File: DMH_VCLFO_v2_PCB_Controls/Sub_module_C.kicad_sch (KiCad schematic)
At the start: 93 parts, among them J46 Conn_02x03_Odd_Even, J47 Conn_02x03_Odd_Even, J48 Conn_02x03_Odd_Even, J49 Conn_02x03_Odd_Even, J50 Conn_02x03_Odd_Even, J51 Conn_02x03_Odd_Even, Q29 BC548, Q30 BC548, Q31 MMBFJ113, Q32 MMBFJ113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

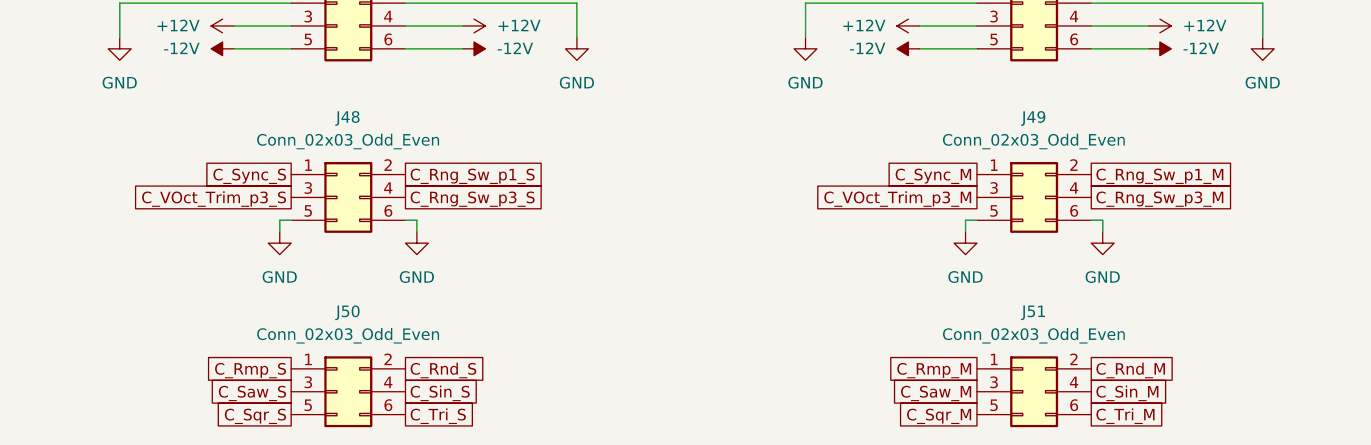
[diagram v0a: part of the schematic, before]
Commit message: Synced Controls PCB with Main
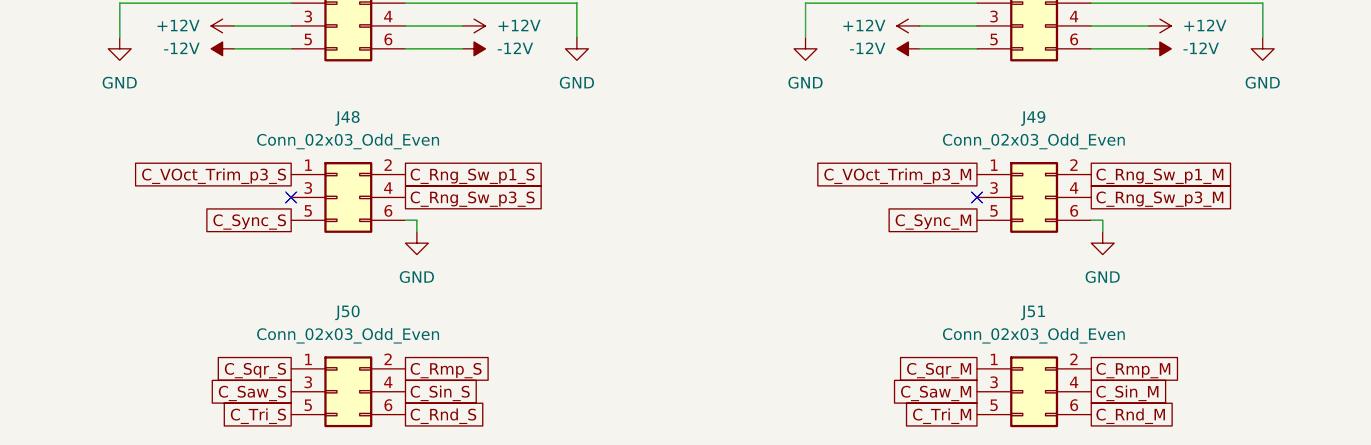
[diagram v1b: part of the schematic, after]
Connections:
- net C_Rmp_M: now also J51.2 (Pin_2); no longer J51.1 (Pin_1)
- net C_Rmp_S: now also J50.2 (Pin_2); no longer J50.1 (Pin_1)
- net C_Rnd_M: now also J51.6 (Pin_6); no longer J51.2 (Pin_2)
- net C_Rnd_S: now also J50.6 (Pin_6); no longer J50.2 (Pin_2)
- net C_Sqr_M: now also J51.1 (Pin_1); no longer J51.5 (Pin_5)
- net C_Sqr_S: now also J50.1 (Pin_1); no longer J50.5 (Pin_5)
- net C_Sync_M: now also J49.5 (Pin_5); no longer J49.1 (Pin_1)
- net C_Sync_S: now also J48.5 (Pin_5); no longer J48.1 (Pin_1)
- net C_Tri_M: now also J51.5 (Pin_5); no longer J51.6 (Pin_6)
- net C_Tri_S: now also J50.5 (Pin_5); no longer J50.6 (Pin_6)
- net C_VOct_Trim_p3_M: now also J49.1 (Pin_1); no longer J49.3 (Pin_3)
- net C_VOct_Trim_p3_S: now also J48.1 (Pin_1); no longer J48.3 (Pin_3)
- net GND: no longer J48.5 (Pin_5), J49.5 (Pin_5)
- no-connect marks 1 -> 3

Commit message: Generated Gerbers
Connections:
- net C_Rnd_S: now also U32.8, U32.9 (-); no longer U32.6 (-), U32.7
- net Comp_Ref: now also U32.2 (-); no longer U32.13 (-)
- net at D22.1 (K): now also U32.1; no longer U32.14
- net at Q31.1 (D), R161.1, R165.1: now also U32.14; no longer U32.1
- net at R161.2, R164.1: now also U32.13 (-); no longer U32.2 (-)
- net at R144.2, R151.1: now also U32.7; no longer U32.8
- net at C39.2, R163.1: now also U32.12 (+); no longer U32.3 (+)
- net at Q29.1 (C), R144.1, R146.2: now also U32.6 (-); no longer U32.9 (-)
- net at Q30.1 (C), R147.2, R156.1: now also U32.5 (+); no longer U32.10 (+)
- net at C42.1, R168.1: now also U32.3 (+); no longer U32.12 (+)
- net at C40.1, Q31.2 (S): now also U32.10 (+); no longer U32.5 (+)
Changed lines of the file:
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@@
 			)
 		)
+		(property "Function" ""
+			(at 243.84 254 0)
+			(effects
+				(font
+					(size 1.27 1.27)
+				)
+			)
+		)
 		(pin "10"
 		)
@@
 		(lib_id "Amplifier_Operational:TL074")
 		(at 69.85 95.25 0)
-		(unit 1)
+		(unit 4)
 		(exclude_from_sim no)
 		(in_bom yes)
@@
 				(path "/58f4306d-5387-4983-bb08-41a2313fd315/04e826af-c525-4e37-8080-dde4fc76eca4"
 					(reference "U32")
-					(unit 1)
+					(unit 4)
 				)
 			)
@@
 		(lib_id "Amplifier_Operational:TL074")
 		(at 69.85 129.54 0)
-		(unit 4)
+		(unit 1)
 		(exclude_from_sim no)
 		(in_bom yes)
@@
 				(path "/58f4306d-5387-4983-bb08-41a2313fd315/04e826af-c525-4e37-8080-dde4fc76eca4"
 					(reference "U32")
-					(unit 4)
+					(unit 1)
 				)
 			)
@@
 		(at 360.68 40.64 0)
 		(mirror x)
-		(unit 3)
+		(unit 2)
 		(exclude_from_sim no)
 		(in_bom yes)
@@
 				(path "/58f4306d-5387-4983-bb08-41a2313fd315/04e826af-c525-4e37-8080-dde4fc76eca4"
 					(reference "U32")
-					(unit 3)
+					(unit 2)
 				)
 			)
@@
 		(lib_id "Amplifier_Operational:TL074")
 		(at 114.3 116.84 0)
-		(unit 2)
+		(unit 3)
 		(exclude_from_sim no)
 		(in_bom yes)
@@
 				(path "/58f4306d-5387-4983-bb08-41a2313fd315/04e826af-c525-4e37-8080-dde4fc76eca4"
 					(reference "U32")
-					(unit 2)
+					(unit 3)
 				)
 			)
